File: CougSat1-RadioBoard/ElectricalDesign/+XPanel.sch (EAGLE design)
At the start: 51 parts, among them J1 ADCS Connector, J2 Low Gain +, J3 Low Gain -, J4 Low Gain Coax, J5 GPS Coax, J6 Picolock Connector, U1 LTC2499, U2 MCP1501-18

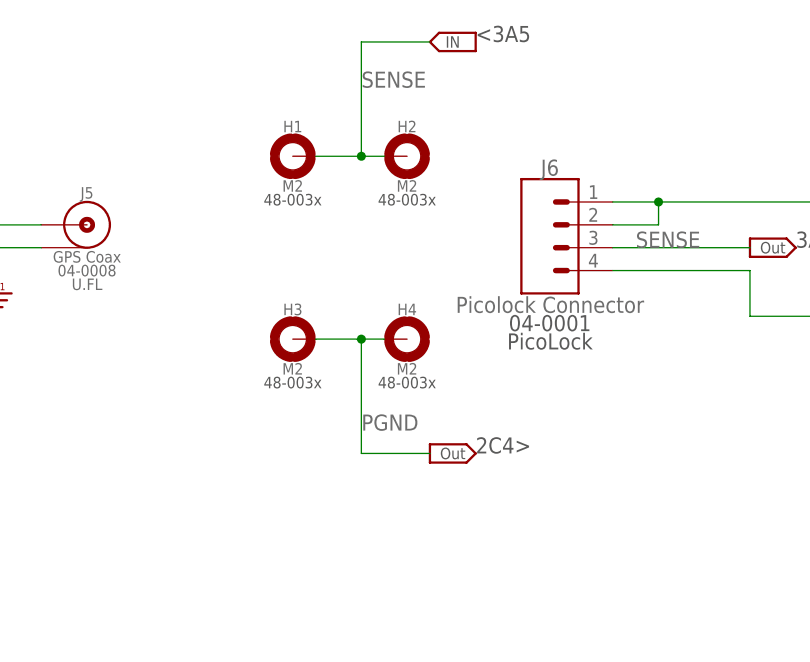
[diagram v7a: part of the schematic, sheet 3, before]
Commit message: Updated connectors
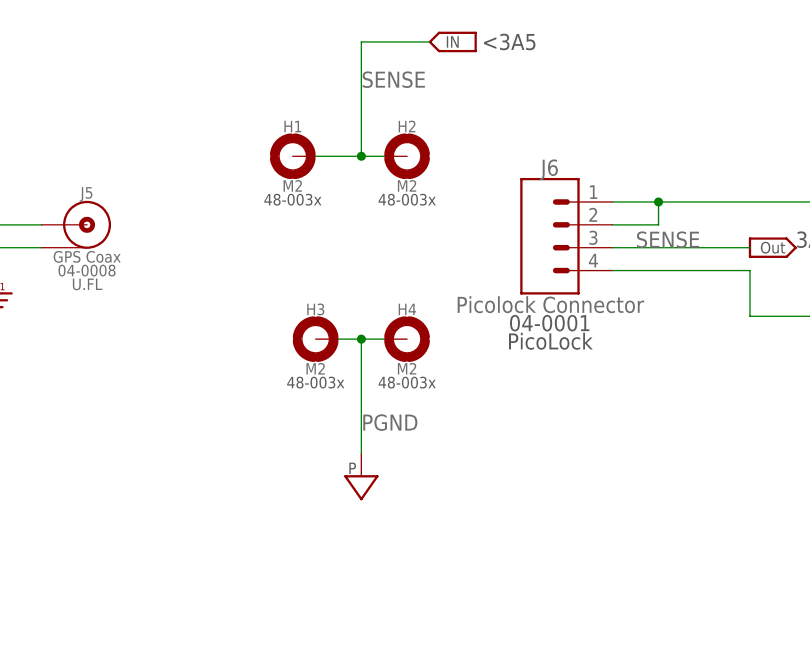
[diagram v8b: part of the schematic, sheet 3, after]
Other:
- note removed: "2C4>"
- moved on the sheet: H3
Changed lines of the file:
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@@
 <part name="OFFSHEET5" library="CougsInSpace-Aesthetics" deviceset="OFF_SHEET-OUT" device=""/>
 <part name="OFFSHEET7" library="CougsInSpace-Aesthetics" deviceset="OFF_SHEET-IN" device=""/>
-<part name="OFFSHEET8" library="CougsInSpace-Aesthetics" deviceset="OFF_SHEET-OUT" device=""/>
 <part name="FRAME4" library="CougsInSpace-Aesthetics" deviceset="FRAME-A" device="">
 <attribute name="TITLE" value="Mechanical"/>
@@
 <part name="SUPPLY50" library="CougsInSpace-PowerSymbols" deviceset="PGND" device=""/>
 <part name="SUPPLY51" library="CougsInSpace-PowerSymbols" deviceset="PGND" device=""/>
+<part name="SUPPLY52" library="CougsInSpace-PowerSymbols" deviceset="PGND" device=""/>
 </parts>
 <sheets>
@@
 <text x="124.46" y="137.16" size="1.778" layer="97" align="center-left">&lt;2A5&gt;</text>
 <text x="124.46" y="139.7" size="1.778" layer="97" align="center-left">&lt;2A5</text>
-<text x="213.36" y="180.34" size="1.778" layer="97" align="center-left">&lt;2B3&gt;</text>
-<text x="213.36" y="177.8" size="1.778" layer="97" align="center-left">  2B3&gt;</text>
-<text x="104.14" y="60.96" size="1.778" layer="97">2B2&gt;</text>
+<text x="213.36" y="180.34" size="1.778" layer="97" align="center-left"> &lt;2B3&gt;</text>
+<text x="213.36" y="177.8" size="1.778" layer="97" align="center-left"> 2B3&gt;</text>
+<text x="104.14" y="60.96" size="1.778" layer="97" align="center-left"> 2B2&gt;</text>
 <text x="38.1" y="38.1" size="1.778" layer="97" align="center">CAD Note: Decoupling</text>
 <wire x1="25.4" y1="63.5" x2="25.4" y2="35.56" width="0.1524" layer="97" style="shortdash"/>
@@
 <sheet>
 <plain>
-<text x="172.72" y="142.24" size="1.778" layer="97">2C4&gt;</text>
-<text x="172.72" y="187.96" size="1.778" layer="97">&lt;3A5</text>
+<text x="172.72" y="187.96" size="1.778" layer="97" align="center-left"> &lt;3A5</text>
 <text x="208.28" y="165.1" size="1.778" layer="97">3A4&gt;</text>
 </plain>
@@
 <attribute name="SKU" x="165.1" y="170.434" size="1.27" layer="97" align="center"/>
 </instance>
-<instance part="H3" gate="G$1" x="152.4" y="154.94" smashed="yes" rot="MR0">
-<attribute name="NAME" x="152.4" y="158.242" size="1.27" layer="95" rot="MR0" align="center"/>
-<attribute name="VALUE" x="152.4" y="151.638" size="1.27" layer="96" rot="MR0" align="center"/>
-<attribute name="SKU" x="152.4" y="150.114" size="1.27" layer="97" rot="MR0" align="center"/>
+<instance part="H3" gate="G$1" x="154.94" y="154.94" smashed="yes" rot="MR0">
+<attribute name="NAME" x="154.94" y="158.242" size="1.27" layer="95" rot="MR0" align="center"/>
+<attribute name="VALUE" x="154.94" y="151.638" size="1.27" layer="96" rot="MR0" align="center"/>
+<attribute name="SKU" x="154.94" y="150.114" size="1.27" layer="97" rot="MR0" align="center"/>
 </instance>
 <instance part="H4" gate="G$1" x="165.1" y="154.94" smashed="yes">
@@
 <instance part="OFFSHEET5" gate="G$1" x="205.74" y="165.1" smashed="yes" rot="MR0"/>
 <instance part="OFFSHEET7" gate="G$1" x="170.18" y="187.96" smashed="yes" rot="MR0"/>
-<instance part="OFFSHEET8" gate="G$1" x="170.18" y="142.24" smashed="yes" rot="R180"/>
 <instance part="H5" gate="G$1" x="38.1" y="109.22" smashed="yes" rot="MR0">
 <attribute name="NAME" x="38.1" y="112.522" size="1.27" layer="95" rot="MR0" align="center"/>
@@
 <instance part="SUPPLY50" gate="G$1" x="180.34" y="66.04" smashed="yes"/>
 <instance part="SUPPLY51" gate="G$1" x="162.56" y="66.04" smashed="yes"/>
+<instance part="SUPPLY52" gate="G$1" x="160.02" y="139.7" smashed="yes"/>
 </instances>
 <busses>
@@
 <pinref part="H3" gate="G$1" pin="MOUNT"/>
 <wire x1="162.56" y1="154.94" x2="160.02" y2="154.94" width="0.1524" layer="91"/>
-<wire x1="160.02" y1="154.94" x2="154.94" y2="154.94" width="0.1524" layer="91"/>
+<wire x1="160.02" y1="154.94" x2="157.48" y2="154.94" width="0.1524" layer="91"/>
 <wire x1="160.02" y1="154.94" x2="160.02" y2="142.24" width="0.1524" layer="91"/>
 <junction x="160.02" y="154.94"/>
 <label x="160.02" y="144.78" size="1.778" layer="95"/>
-<wire x1="160.02" y1="142.24" x2="167.64" y2="142.24" width="0.1524" layer="91"/>
-</segment>
-<segment>
+<pinref part="SUPPLY52" gate="G$1" pin="PGND"/>
+</segment>
+<segment>
